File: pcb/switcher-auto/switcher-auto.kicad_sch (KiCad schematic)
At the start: 23 parts, among them J0 MD-90SM, J5 Conn_02x22_Top_Bottom, SW1 SW_Push, SW2 SW_Push, U1 CD74HC4067SM96, U2 CD74HC4067SM96, U3 CD74HC4067SM96, U4 CD74HC4067SM96, U5 CD74HC4067SM96, U6 CD74HC4067SM96, U7 CD74HC4067SM96

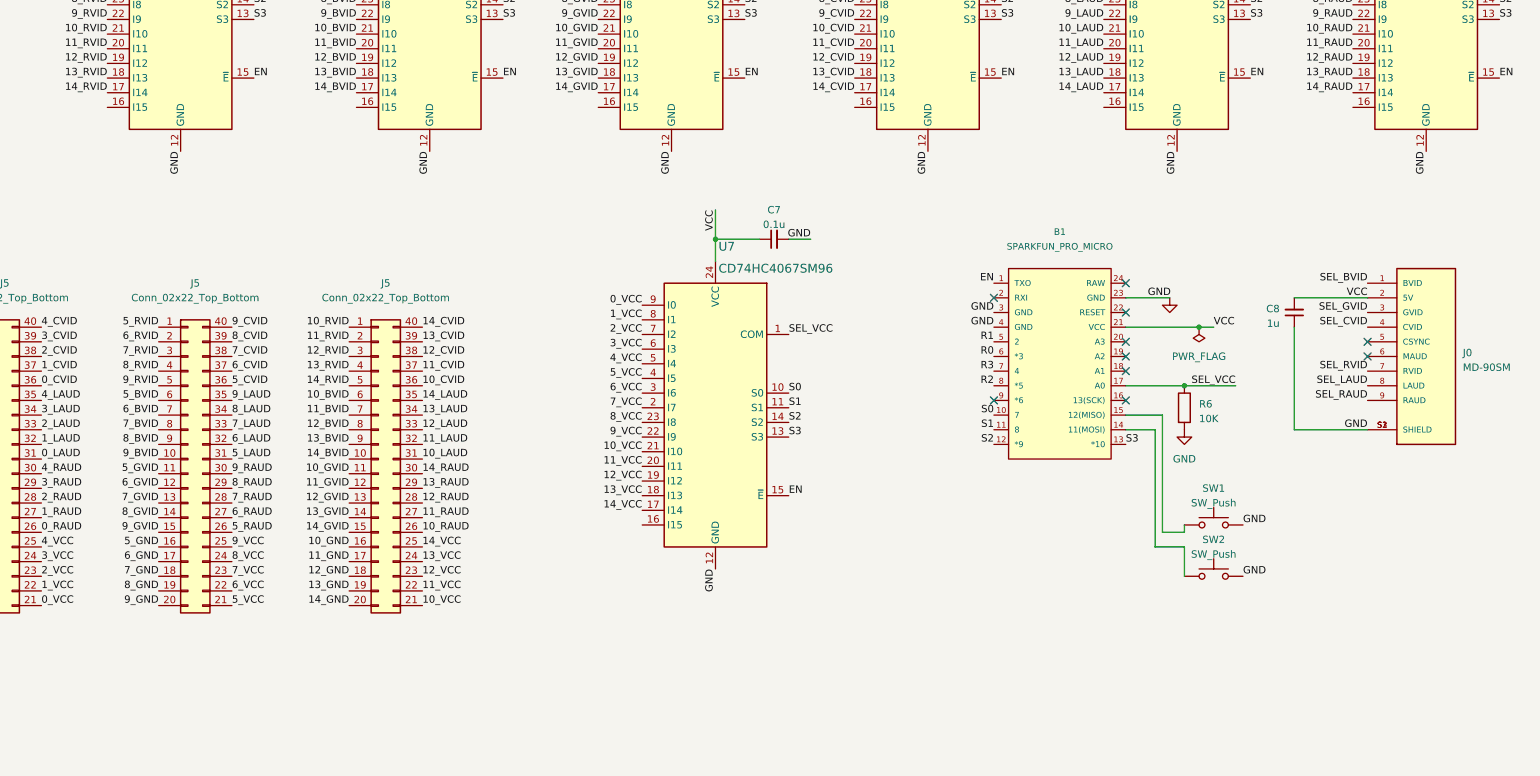
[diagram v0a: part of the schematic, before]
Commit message: Finishing routing
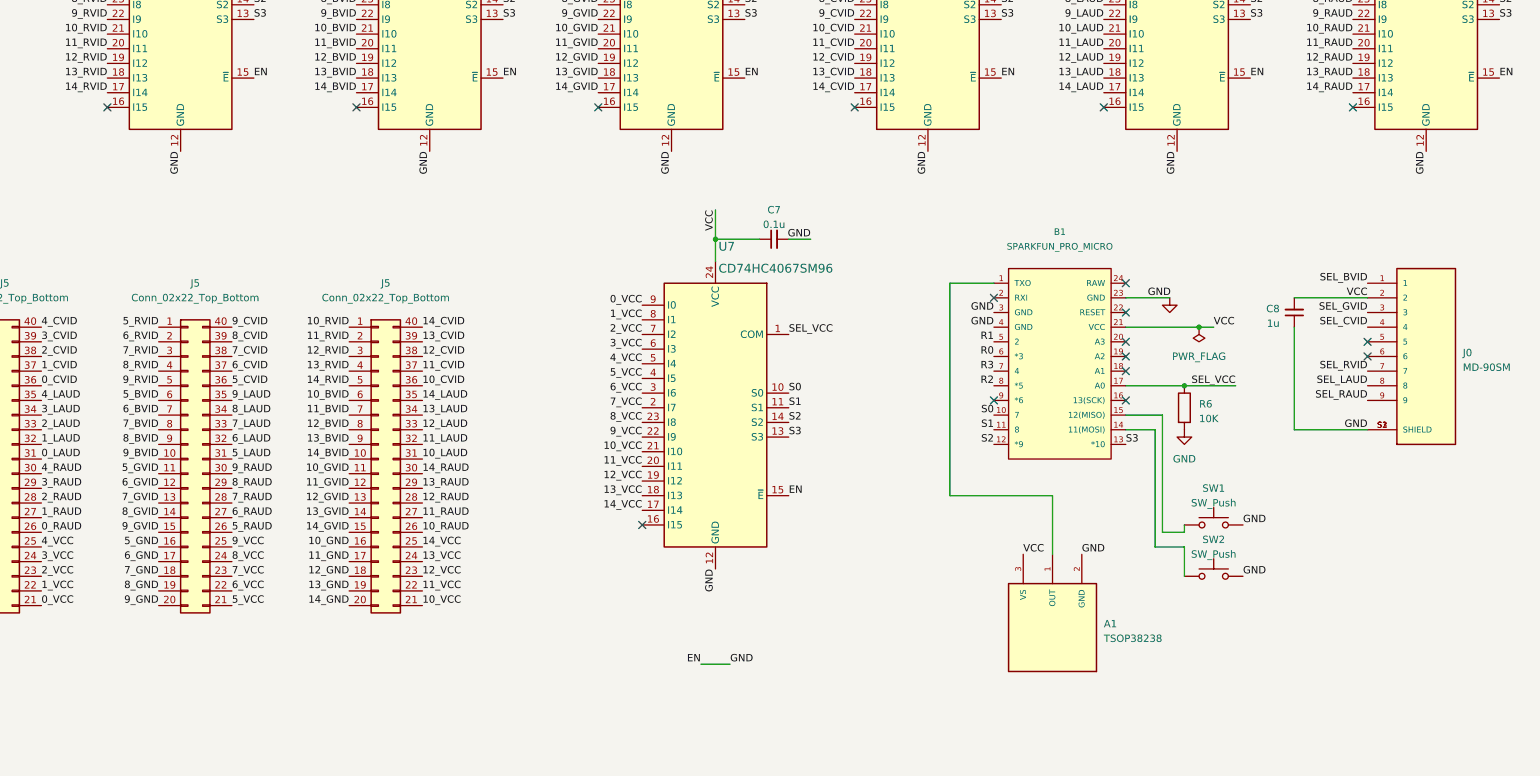
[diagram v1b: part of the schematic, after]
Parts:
- added A1: TSOP38238, XDCR_TSOP38238, symbol REB-IR:TSOP38238
- J0: footprint DIN9:CUI_MD-90SM -> CUI_MD-90SM; symbol DIN9:MD-90SM -> REB-DIN:MD-90SM
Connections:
- net GND: now also U1.15 (~{E}), U2.15 (~{E}), U3.15 (~{E}), U4.15 (~{E}), U5.15 (~{E}), U6.15 (~{E}), U7.15 (~{E}), A1.2 (GND)
- net VCC: now also A1.3 (VS)
- removed net EN: B1.1 (TXO), U1.15 (~{E}), U2.15 (~{E}), U3.15 (~{E}), U4.15 (~{E}), U5.15 (~{E}), U6.15 (~{E}), U7.15 (~{E})
- new net: A1.1 (OUT), B1.1 (TXO)
- no-connect marks 10 -> 17
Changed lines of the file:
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@@
   (no_connect (at 207.01 129.54))
   (no_connect (at 229.87 119.38))
+  (no_connect (at 226.06 78.74))
   (no_connect (at 207.01 111.76))
+  (no_connect (at 138.43 78.74))
   (no_connect (at 271.78 119.38))
+  (no_connect (at 96.52 78.74))
+  (no_connect (at 146.05 151.13))
+  (no_connect (at 182.88 78.74))
+  (no_connect (at 269.24 78.74))
+  (no_connect (at 53.34 78.74))
   (no_connect (at 229.87 114.3))
   (wire (pts (xy 151.13 17.78) (xy 151.13 26.67))
     (stroke (width 0) (type default))
   )
+  (wire (pts (xy 217.17 146.05) (xy 217.17 156.21))
+    (stroke (width 0) (type default))
+  )
   (wire (pts (xy 259.08 134.62) (xy 271.78 134.62))
     (stroke (width 0) (type default))
@@
     (stroke (width 0) (type default))
   )
+  (wire (pts (xy 156.21 175.26) (xy 161.29 175.26))
+    (stroke (width 0) (type default))
+  )
   (wire (pts (xy 368.3 33.02) (xy 368.3 91.44))
     (stroke (width 0) (type default))
@@
     (stroke (width 0) (type default))
   )
+  (wire (pts (xy 199.39 109.22) (xy 199.39 146.05))
+    (stroke (width 0) (type default))
+  )
   (wire (pts (xy 71.12 27.94) (xy 74.93 27.94))
     (stroke (width 0) (type default))
@@
     (stroke (width 0) (type default))
   )
+  (wire (pts (xy 199.39 146.05) (xy 217.17 146.05))
+    (stroke (width 0) (type default))
+  )
   (wire (pts (xy 240.03 127) (xy 248.92 127))
     (stroke (width 0) (type default))
@@
     (stroke (width 0) (type default))
   )
+  (wire (pts (xy 207.01 109.22) (xy 199.39 109.22))
+    (stroke (width 0) (type default))
+  )
   (label "12_VCC" (at 146.05 143.51 180) (fields_autoplaced)
     (effects (font (size 1.27 1.27)) (justify right bottom))
@@
     (effects (font (size 1.27 1.27)) (justify right bottom))
   )
+  (label "GND" (at 222.25 156.21 0) (fields_autoplaced)
+    (effects (font (size 1.27 1.27)) (justify left bottom))
+  )
   (label "12_GVID" (at 95.25 147.32 180) (fields_autoplaced)
     (effects (font (size 1.27 1.27)) (justify right bottom))
@@
     (effects (font (size 1.27 1.27)) (justify left bottom))
   )
+  (label "GND" (at 161.29 175.26 0) (fields_autoplaced)
+    (effects (font (size 1.27 1.27)) (justify left bottom))
+  )
   (label "0_BVID" (at 96.52 40.64 180) (fields_autoplaced)
     (effects (font (size 1.27 1.27)) (justify right bottom))
@@
     (effects (font (size 1.27 1.27)) (justify right bottom))
   )
+  (label "EN" (at 156.21 175.26 180) (fields_autoplaced)
+    (effects (font (size 1.27 1.27)) (justify right bottom))
+  )
   (label "10_RVID" (at 53.34 66.04 180) (fields_autoplaced)
     (effects (font (size 1.27 1.27)) (justify right bottom))
@@
     (effects (font (size 1.27 1.27)) (justify right bottom))
   )
-  (label "EN" (at 207.01 109.22 180) (fields_autoplaced)
-    (effects (font (size 1.27 1.27)) (justify right bottom))
-  )
   (label "12_CVID" (at 182.88 71.12 180) (fields_autoplaced)
     (effects (font (size 1.27 1.27)) (justify right bottom))
@@
   (label "9_GVID" (at 138.43 63.5 180) (fields_autoplaced)
     (effects (font (size 1.27 1.27)) (justify right bottom))
+  )
+  (label "VCC" (at 212.09 156.21 0) (fields_autoplaced)
+    (effects (font (size 1.27 1.27)) (justify left bottom))
   )
   (label "0_RVID" (at 29.21 116.84 180) (fields_autoplaced)
@@
         (path "/e72d49f3-4a7e-4284-a905-90a44014e1f4"
           (reference "#PWR02") (unit 1)
+        )
+      )
+    )
+  )
+  (symbol (lib_id "REB-IR:TSOP38238") (at 217.17 168.91 90) (unit 1)
+    (in_bom yes) (on_board yes) (dnp no) (fields_autoplaced)
+    (property "Reference" "A1" (at 226.06 168.275 90)
+      (effects (font (size 1.27 1.27)) (justify right))
+    )
+    (property "Value" "TSOP38238" (at 226.06 170.815 90)
+      (effects (font (size 1.27 1.27)) (justify right))
+    )
+    (property "Footprint" "XDCR_TSOP38238" (at 217.17 168.91 0)
+      (effects (font (size 1.27 1.27)) (justify bottom) hide)
+    )
+    (property "Datasheet" "" (at 217.17 168.91 0)
+      (effects (font (size 1.27 1.27)) hide)
+    )
+    (property "PARTREV" "1.7" (at 217.17 168.91 0)
+      (effects (font (size 1.27 1.27)) (justify bottom) hide)
+    )
+    (property "STANDARD" "Manufacturer Recommendations" (at 217.17 168.91 0)
+      (effects (font (size 1.27 1.27)) (justify bottom) hide)
+    )
+    (property "MAXIMUM_PACKAGE_HEIGHT" "10.55 mm" (at 217.17 168.91 0)
+      (effects (font (size 1.27 1.27)) (justify bottom) hide)
+    )
+    (property "MANUFACTURER" "Vishay" (at 217.17 168.91 0)
+      (effects (font (size 1.27 1.27)) (justify bottom) hide)
+    )
+    (pin "1")
+    (pin "2")
+    (pin "3")
+    (instances
+      (project "switcher-auto"
+        (path "/e72d49f3-4a7e-4284-a905-90a44014e1f4"
+          (reference "A1") (unit 1)
         )
       )
@@
     )
   )
-  (symbol (lib_name "MD-90SM_1") (lib_id "DIN9:MD-90SM") (at 281.94 121.92 0) (unit 1)
+  (symbol (lib_id "REB-DIN:MD-90SM") (at 281.94 121.92 0) (unit 1)
     (in_bom yes) (on_board yes) (dnp no) (fields_autoplaced)
     (property "Reference" "J0" (at 288.29 121.285 0)
@@
       (effects (font (size 1.27 1.27)) (justify left))
     )
-    (property "Footprint" "DIN9:CUI_MD-90SM" (at 281.94 102.87 0)
+    (property "Footprint" "CUI_MD-90SM" (at 281.94 121.92 0)
       (effects (font (size 1.27 1.27)) (justify bottom) hide)
     )
@@
       (effects (font (size 1.27 1.27)) hide)
     )
-    (property "STANDARD" "Manufacturer Recommendations" (at 275.59 111.76 0)
-      (effects (font (size 1.27 1.27)) (justify left bottom) hide)
-    )
-    (property "PARTREV" "02/18/2022" (at 275.59 109.22 0)
-      (effects (font (size 1.27 1.27)) (justify left bottom) hide)
-    )
-    (property "MANUFACTURER" "CUI" (at 275.59 114.3 0)
-      (effects (font (size 1.27 1.27)) (justify left bottom) hide)
-    )
-    (property "MAXIMUM_PACKAGE_HEIGHT" "13.6 mm" (at 275.59 116.84 0)
-      (effects (font (size 1.27 1.27)) (justify left bottom) hide)
+    (property "STANDARD" "Manufacturer Recommendations" (at 281.94 121.92 0)
+      (effects (font (size 1.27 1.27)) (justify bottom) hide)
+    )
+    (property "PARTREV" "02/18/2022" (at 281.94 121.92 0)
+      (effects (font (size 1.27 1.27)) (justify bottom) hide)
+    )
+    (property "MANUFACTURER" "CUI" (at 281.94 121.92 0)
+      (effects (font (size 1.27 1.27)) (justify bottom) hide)
+    )
+    (property "MAXIMUM_PACKAGE_HEIGHT" "13.6 mm" (at 281.94 121.92 0)
+      (effects (font (size 1.27 1.27)) (justify bottom) hide)
     )
     (property "Notes" "" (at 281.94 121.92 0)

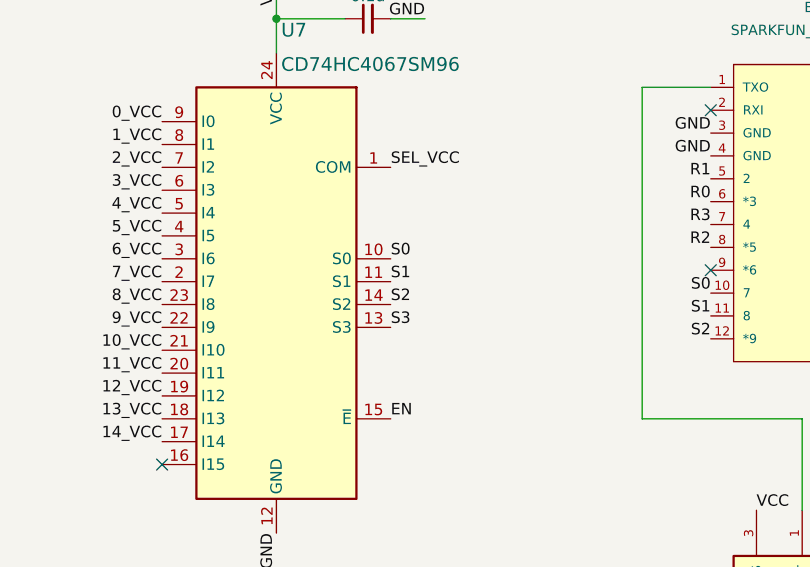
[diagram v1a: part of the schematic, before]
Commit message: Hooks up V sense muxer
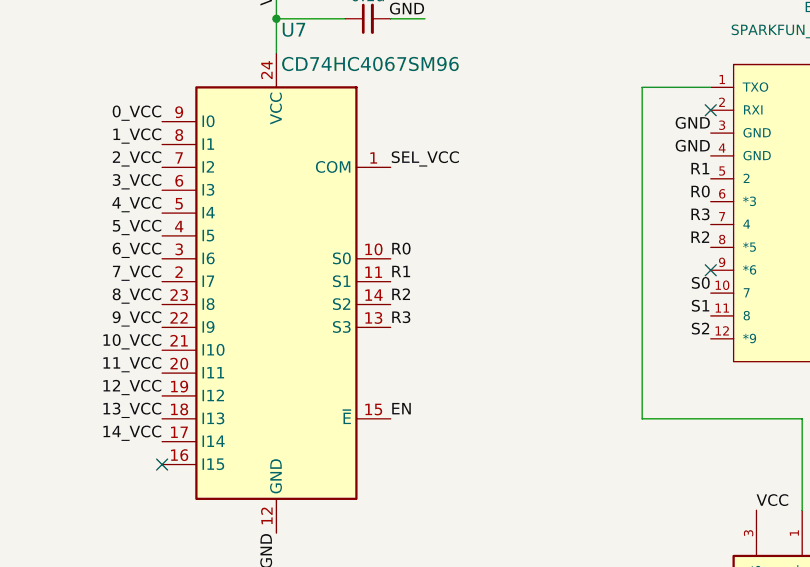
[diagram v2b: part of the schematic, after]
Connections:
- net R0: now also U7.10 (S0)
- net R1: now also U7.11 (S1)
- net R2: now also U7.14 (S2)
- net R3: now also U7.13 (S3)
- net S0: no longer U7.10 (S0)
- net S1: no longer U7.11 (S1)
- net S2: no longer U7.14 (S2)
- net S3: no longer U7.13 (S3)
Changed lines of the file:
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@@
     (effects (font (size 1.27 1.27)) (justify left bottom))
   )
-  (label "S0" (at 171.45 128.27 0) (fields_autoplaced)
+  (label "R0" (at 171.45 128.27 0) (fields_autoplaced)
     (effects (font (size 1.27 1.27)) (justify left bottom))
   )
@@
     (effects (font (size 1.27 1.27)) (justify right bottom))
   )
-  (label "S1" (at 171.45 130.81 0) (fields_autoplaced)
+  (label "R1" (at 171.45 130.81 0) (fields_autoplaced)
     (effects (font (size 1.27 1.27)) (justify left bottom))
   )
@@
     (effects (font (size 1.27 1.27)) (justify right bottom))
   )
-  (label "S2" (at 171.45 133.35 0) (fields_autoplaced)
+  (label "R2" (at 171.45 133.35 0) (fields_autoplaced)
     (effects (font (size 1.27 1.27)) (justify left bottom))
   )
@@
     (effects (font (size 1.27 1.27)) (justify right bottom))
   )
-  (label "S3" (at 171.45 135.89 0) (fields_autoplaced)
-    (effects (font (size 1.27 1.27)) (justify left bottom))
-  )
+  (label "R3" (at 171.45 135.89 0) (fields_autoplaced)
+    (effects (font (size 1.27 1.27)) (justify left bottom))
+  )

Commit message: Adds daughterboard with adjustment options
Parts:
- A1: footprint XDCR_TSOP38238 -> REB-IR:XDCR_TSOP38238
- J0: footprint CUI_MD-90SM -> DIN9:CUI_MD-90SM
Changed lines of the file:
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@@
       (effects (font (size 1.27 1.27)) (justify right))
     )
-    (property "Footprint" "XDCR_TSOP38238" (at 217.17 168.91 0)
+    (property "Footprint" "REB-IR:XDCR_TSOP38238" (at 217.17 168.91 0)
       (effects (font (size 1.27 1.27)) (justify bottom) hide)
     )
@@
       (effects (font (size 1.27 1.27)) (justify left))
     )
-    (property "Footprint" "CUI_MD-90SM" (at 281.94 121.92 0)
+    (property "Footprint" "DIN9:CUI_MD-90SM" (at 281.94 121.92 0)
       (effects (font (size 1.27 1.27)) (justify bottom) hide)
     )
